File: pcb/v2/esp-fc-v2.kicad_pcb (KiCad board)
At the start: 2 copper layers, 0 parts

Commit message: pcb v2: 36x36 4-layer outline, JLC rules, two-sided placement, GND/3V3/5V planes
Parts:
- added C1: 10uF 50V X7R, Capacitor_SMD:C_1206_3216Metric, F.Cu at (112.9, 105.6)
- added C10: 10uF 10V, Capacitor_SMD:C_0805_2012Metric, B.Cu at (106.0, 108.5)
- added C11: 22uF 10V, Capacitor_SMD:C_0805_2012Metric, F.Cu at (89.8, 87.0)
- added C12: 100nF, Capacitor_SMD:C_0603_1608Metric, F.Cu at (89.8, 83.8)
- added C13: 1uF, Capacitor_SMD:C_0603_1608Metric, B.Cu at (93.4, 89.7)
- added C14: 100nF, Capacitor_SMD:C_0603_1608Metric, B.Cu at (104.8, 96.6)
- added C15: 2.2uF, Capacitor_SMD:C_0603_1608Metric, B.Cu at (104.8, 101.4)
- added C16: 10nF, Capacitor_SMD:C_0603_1608Metric, B.Cu at (107.4, 99.0)
- added C17: 100nF, Capacitor_SMD:C_0603_1608Metric, B.Cu at (100.0, 102.0)
- added C18: 100nF, Capacitor_SMD:C_0603_1608Metric, B.Cu at (102.6, 104.0)
- added C2: 10uF 50V X7R, Capacitor_SMD:C_1206_3216Metric, F.Cu at (115.9, 105.6)
- added C3: 100nF 50V, Capacitor_SMD:C_0603_1608Metric, B.Cu at (114.6, 103.5)
- added C4: 1uF 16V, Capacitor_SMD:C_0603_1608Metric, B.Cu at (109.8, 97.0)
- added C5: 100nF, Capacitor_SMD:C_0603_1608Metric, B.Cu at (109.8, 95.0)
- added C6: 22uF 16V X5R, Capacitor_SMD:C_1206_3216Metric, B.Cu at (112.9, 91.2)
- added C7: 22uF 16V X5R, Capacitor_SMD:C_1206_3216Metric, B.Cu at (115.9, 91.2)
- added C8: 100nF, Capacitor_SMD:C_0603_1608Metric, B.Cu at (96.6, 89.7)
- added C9: 10uF 10V, Capacitor_SMD:C_0805_2012Metric, B.Cu at (102.3, 108.5)
- added D1: SMAJ20A, Diode_SMD:D_SMA, F.Cu at (92.2, 108.0)
- added D2: B5819W, Diode_SMD:D_SOD-123, B.Cu at (88.3, 106.6)
- added D3: RED, LED_SMD:LED_0603_1608Metric, F.Cu at (107.5, 105.0)
- added D4: GREEN, LED_SMD:LED_0603_1608Metric, F.Cu at (107.5, 108.8)
- added D5: 1N4148W, Diode_SMD:D_SOD-323, B.Cu at (114.6, 106.6)
- added FB1: 600R@100MHz, Inductor_SMD:L_0603_1608Metric, B.Cu at (107.4, 102.4)
- added H1: M3, MountingHole:MountingHole_3.2mm_M3, F.Cu at (84.8, 84.8)
- added H2: M3, MountingHole:MountingHole_3.2mm_M3, F.Cu at (115.2, 84.8)
- added H3: M3, MountingHole:MountingHole_3.2mm_M3, F.Cu at (115.2, 115.2)
- added H4: M3, MountingHole:MountingHole_3.2mm_M3, F.Cu at (84.8, 115.2)
- added J1: ESC_4in1_SH8, Connector_JST:JST_SH_SM08B-SRSS-TB_1x08-1MP_P1.00mm_Horizontal, F.Cu at (100.0, 114.5)
- added J2: USB-C, Connector_USB:USB_C_Receptacle_HRO_TYPE-C-31-M-12, F.Cu at (86.3, 96.0)
- added J3: RX_CRSF, Connector_JST:JST_SH_SM04B-SRSS-TB_1x04-1MP_P1.00mm_Horizontal, B.Cu at (105.0, 85.6)
- added J4: GPS_MAG, Connector_JST:JST_SH_SM06B-SRSS-TB_1x06-1MP_P1.00mm_Horizontal, B.Cu at (94.2, 85.6)
- added L1: 4.7uH Isat>=3A (SWPA5020S4R7MT), Inductor_SMD:L_Sunlord_SWPA5020S, F.Cu at (114.6, 91.4)
- added Q1: MMBT3904, Package_TO_SOT_SMD:SOT-23, B.Cu at (93.0, 104.5)
- added Q2: MMBT3904, Package_TO_SOT_SMD:SOT-23, B.Cu at (97.2, 104.5)
- added Q3: 2N7002, Package_TO_SOT_SMD:SOT-23, B.Cu at (109.6, 106.0)
- added R1: 100k 1%, Resistor_SMD:R_0603_1608Metric, B.Cu at (109.8, 101.0)
- added R10: 10k, Resistor_SMD:R_0603_1608Metric, B.Cu at (103.2, 89.7)
- added R11: 4.7k, Resistor_SMD:R_0603_1608Metric, B.Cu at (106.3, 89.7)
- added R12: 4.7k, Resistor_SMD:R_0603_1608Metric, B.Cu at (109.4, 89.7)
- added R13: 100k 1%, Resistor_SMD:R_0603_1608Metric, B.Cu at (100.0, 98.0)
- added R14: 10k 1%, Resistor_SMD:R_0603_1608Metric, B.Cu at (100.0, 100.0)
- added R15: 100k, Resistor_SMD:R_0603_1608Metric, B.Cu at (109.6, 109.0)
- added R16: 330, Resistor_SMD:R_0603_1608Metric, B.Cu at (106.3, 111.0)
- added R17: 0R (CH340 V3 tie, datasheet 3.3V mode), Resistor_SMD:R_0603_1608Metric, B.Cu at (100.0, 96.0)
- added R2: 24.9k 1%, Resistor_SMD:R_0603_1608Metric, B.Cu at (109.8, 103.0)
- added R3: 5.1k, Resistor_SMD:R_0603_1608Metric, B.Cu at (84.0, 102.5)
- added R4: 5.1k, Resistor_SMD:R_0603_1608Metric, B.Cu at (84.0, 106.4)
- added R5: 10k, Resistor_SMD:R_0603_1608Metric, B.Cu at (93.0, 107.6)
- added R6: 10k, Resistor_SMD:R_0603_1608Metric, B.Cu at (97.2, 107.6)
- added R7: 10k, Resistor_SMD:R_0603_1608Metric, B.Cu at (90.4, 89.7)
- added R8: 1k, Resistor_SMD:R_0603_1608Metric, F.Cu at (107.5, 106.9)
- added R9: 1k, Resistor_SMD:R_0603_1608Metric, F.Cu at (107.5, 110.6)
- added SW1: RESET, Button_Switch_SMD:SW_Push_1P1T_NO_CK_KMR2, B.Cu at (95.0, 115.5)
- added SW2: BOOT, Button_Switch_SMD:SW_Push_1P1T_NO_CK_KMR2, B.Cu at (101.0, 115.5)
- added TP1: VBAT_PAD, TestPoint:TestPoint_Pad_2.5x2.5mm, F.Cu at (85.0, 106.0)
- added TP2: GND_PAD, TestPoint:TestPoint_Pad_2.5x2.5mm, F.Cu at (85.0, 109.9)
- added TP3: BUZ+, TestPoint:TestPoint_Pad_1.5x1.5mm, B.Cu at (113.5, 109.6)
- added TP4: BUZ-, TestPoint:TestPoint_Pad_1.5x1.5mm, B.Cu at (116.3, 109.6)
- added TP5: LED_DIN, TestPoint:TestPoint_Pad_1.5x1.5mm, B.Cu at (109.6, 112.6)
- added U1: LMR33630BDDA, Package_SO:Texas_HSOP-8-1EP_3.9x4.9mm_P1.27mm_ThermalVias, F.Cu at (114.6, 98.6)
- added U2: USBLC6-2SC6, Package_TO_SOT_SMD:SOT-23-6, B.Cu at (88.5, 103.2)
- added U3: CH340C, Package_SO:SOIC-16_3.9x9.9mm_P1.27mm, B.Cu at (94.5, 97.5)
- added U4: AP7361C-33E, Package_TO_SOT_SMD:SOT-223-3_TabPin2, F.Cu at (100.9, 107.4)
- added U5: ESP32-WROOM-32UE-N4, RF_Module:ESP32-WROOM-32UE, F.Cu at (101.5, 93.2)
- added U6: ICM-42688-P, Package_LGA:LGA-14_3x2.5mm_P0.5mm_LayoutBorder3x4y, B.Cu at (104.8, 99.0)
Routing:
- added copper zone on In2.Cu, net +3V3
- added copper zone on In2.Cu, net +5V
- added copper zone on B.Cu, net GND
- added copper zone on F.Cu, net GND
- added copper zone on In1.Cu, net GND
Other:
- board outline added: 36 x 36 mm
- copper layers 2 -> 4

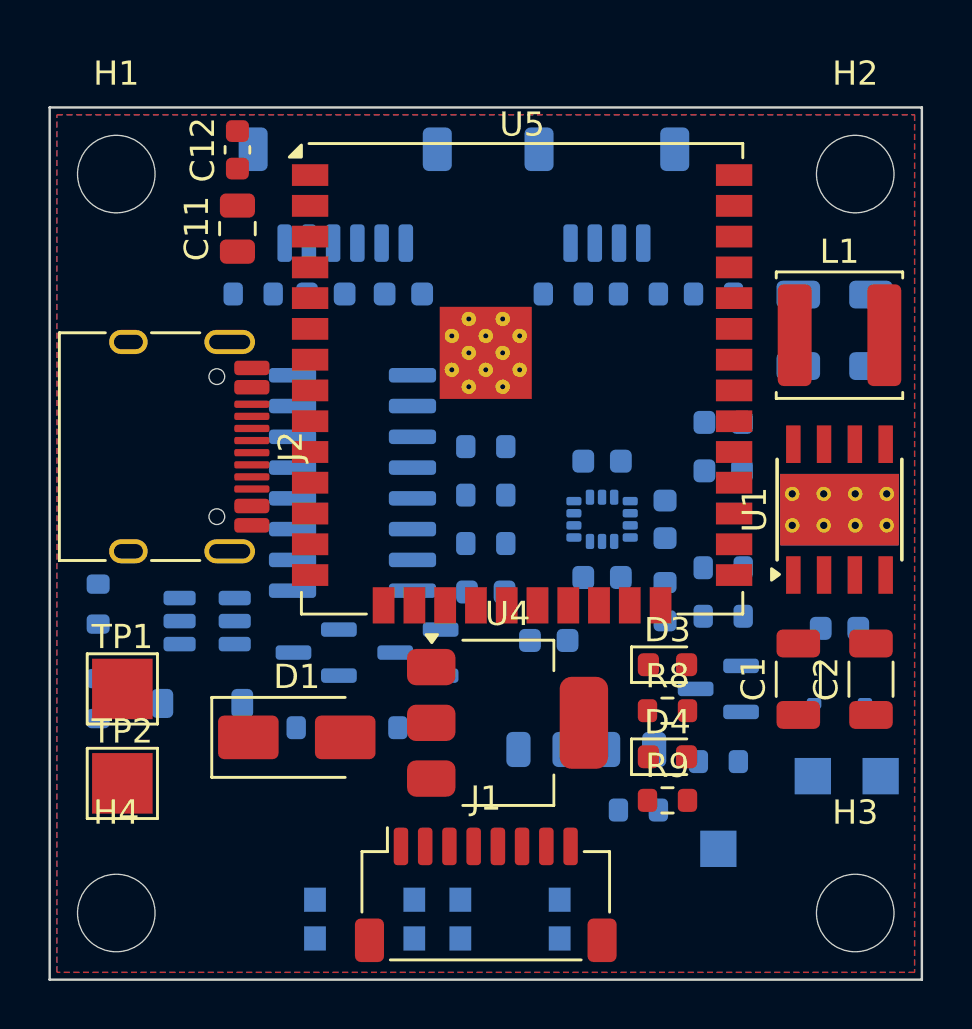
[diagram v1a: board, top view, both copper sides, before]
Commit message: pcb v2: routed (In1 solid GND, In2 3V3 plane, GND stitching); DRC/ERC reports
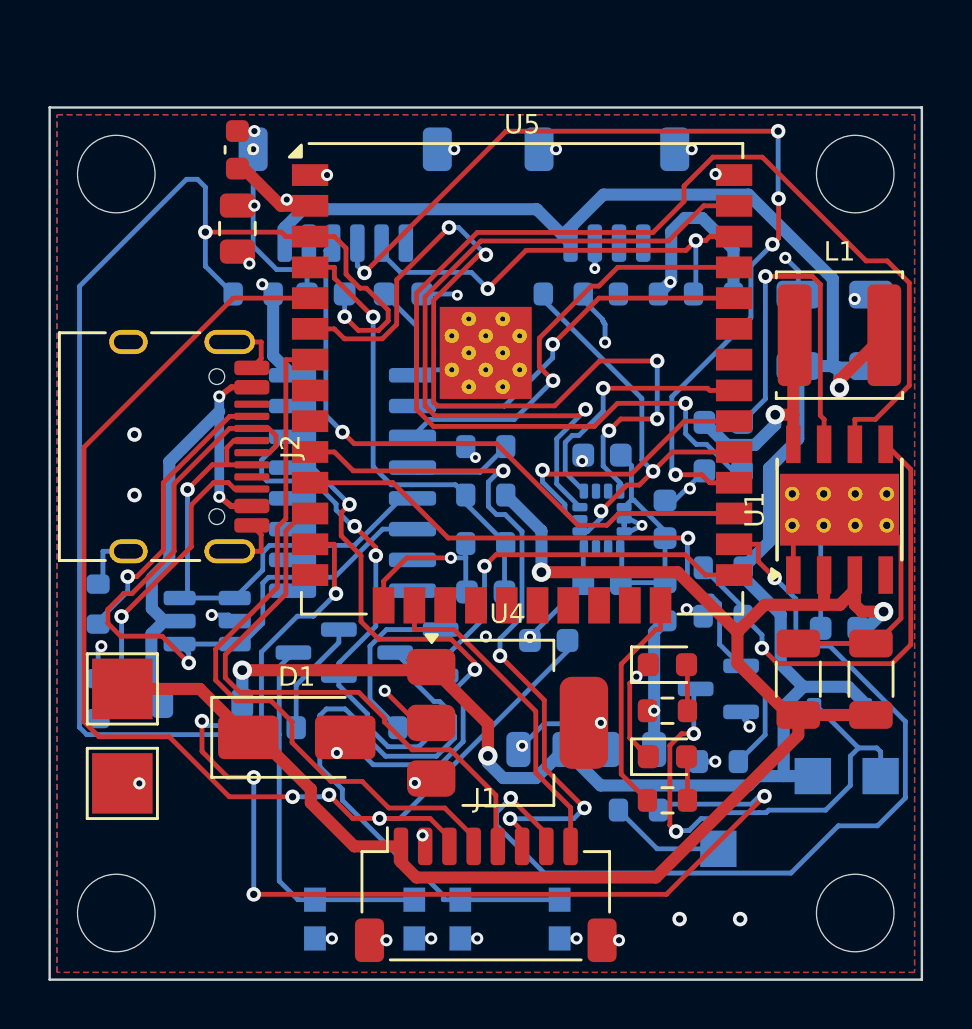
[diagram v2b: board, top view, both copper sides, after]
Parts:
- moved C14 0.25 mm to (104.8, 96.3)
- moved C15 0.25 mm to (104.8, 101.7)
- turned U6 to -90 degrees
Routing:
- net GND: track 0.00 -> 95.2 mm, vias 0 -> 39
- net +5V: track 0.00 -> 88.2 mm, vias 0 -> 3
- net EN: track 0.00 -> 67.3 mm, vias 0 -> 2
- net VBAT: track 0.00 -> 66.3 mm, vias 0 -> 2
- net BUCK_VCC: track 0.00 -> 54.1 mm, vias 0 -> 1
- net CURR_ADC: track 0.00 -> 51.8 mm, vias 0 -> 3
- net LED_STRIP: track 0.00 -> 48.6 mm, vias 0 -> 5
- net IO0: track 0.00 -> 43.1 mm, vias 0 -> 1
- net UART2_TX: track 0.00 -> 39.5 mm, vias 0 -> 5
- net M3: track 0.00 -> 37.4 mm, vias 0 -> 2
- net GYRO_INT: track 0.00 -> 35.5 mm, vias 0 -> 5
- net USB_DN: track 0.00 -> 31.4 mm, vias 0 -> 1
- net SPI_MOSI: track 0.00 -> 30.6 mm, vias 0 -> 1
- net M2: track 0.00 -> 29.8 mm, vias 0 -> 4
- net ESC_TLM: track 0.00 -> 29.7 mm
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- removed copper zone on In2.Cu, net +5V
